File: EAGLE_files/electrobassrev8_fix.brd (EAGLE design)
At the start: 301.8 x 129.5 mm, 234 parts, among them IC1 CY8C58LPXXX, IC18 CY8C4124, IC2 4052D, IC3 LMV321M5, IC5 LMV321M5, IC6 LM324D, J1 105162-0001, J28 PJ-066A, Q1 DMP3099L, U1 ES_DAISY_SEED_DOUBLE, U2 LP2985, U7 ES_DAISY_SEED_DOUBLE, X1 3P-2MM-TH-MALE, X10 3P-2MM-TH-MALE, X11 3P-2MM-TH-MALE, X12 3P-2MM-TH-MALE, X13 3P-2MM-TH-MALE, X14 3P-2MM-TH-MALE, X15 3P-2MM-TH-MALE, X16 332-02, X17 332-02, X18 332-02, X19 332-02, X2 NRJ6HF2, X3 NRJ6HF2, X4 USB+SHIELD, X5 332-02, X6 332-02, X7 332-02, X8 332-02, X9 3P-2MM-TH-MALE

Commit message: changes to how presets are loaded
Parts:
- removed 0_6: (no value), adafruit:1X01
- removed IC1: CY8C58LPXXX, cypress:TQFP100-14X14
- removed JP17, JP18, JP19: PINHD-2X5, Connector:2X05
- removed JP20, JP21: 20021121, custom:20021121
- removed R47, R51, R52, R53, R54: 0R_DNP, adafruit:R0603
- removed U$7: CY8CKIT-059_TARGET_3, CY8KIT-059:CY8CKIT-059_TARGET_3
- added 12VD1: (no value), adafruit:1X01
- added C15, C19, C22, C23, C24, C25: 10uf, rcl:C1206K
- added C16, C31, C32, C33, C36, C45, C46: 1uf, rcl:C0603
- added C17: .001uf, rcl:C0603
- added C18: .01uf, adafruit:C0603K
- added C20, C21: 22uf, rcl:C1206K
- added C26, C28, C30, C40, C41, C42, C43, C44: .1uf, rcl:C0603K
- added C29: 2200pf, adafruit:C0603K
- added J2, J3, J5, J6, J7, J8: SM06B-SRSS-TB(LF)(SN), sm06b:CONN_SM06B-SRSS-TB_JST
- added JP5: 20021121, custom:20021121
- added L1: 2.2uH, Electrosmith-Passives:BOURNS_SRP2010
- added R27, R36: 20k, Resistor:R0603
- added R34, R35: 10k, Resistor:R0603
- added R37: 22R, rcl:R0603
- added R56, R57, R88, R89, R90: 2M, Electrosmith-Passives:R0603
- added R91, R92: 100R, Electrosmith-Passives:R0603
- added R93, R94, R95, R96, R97: 47k, rcl:R0603
- added U$9: POWER_ISOLATE, Electrosmith-IC:XP_POWER_ISEXXXXA
- added U10: OPA1654, Electrosmith-IC:TSSOP-14
- added U3: MCP1755T-5002E/DCSOT-223_5_MCH-M, MCP1755T:SOT-223_5_MCH-M
- added U4: CY8C5888LTI-LP097QFN-68-M, cy8c:QFN-68-M
- added U5: ADUM3160BRWZRW_16_ADI-M, MCP1755T:RW_16_ADI-M
- R23: value 0R -> 2M; device adafruit:R0603 -> Electrosmith-Passives:R0603
- R32: value 1.6k -> 5R_DNP
- R41: value 1.6k -> 22R; device adafruit:R0603 -> rcl:R0603
- R45, R46: value 0R_DNP -> 22R; device adafruit:R0603 -> rcl:R0603
- R50: value 0R -> 5R
- moved R41 113.5 mm to (240.0, 30.0), turned to 0 degrees
- moved R32 99.7 mm to (233.4, 76.2), turned to 90 degrees
- moved C11 59.1 mm to (175.3, 66.5), turned to 270 degrees
- moved R25 56.3 mm to (170.7, 65.5), turned to 180 degrees
- moved C34 55.1 mm to (46.2, 59.9)
- moved R26 52.5 mm to (170.2, 74.7), turned to 180 degrees
- moved C4 52.2 mm to (186.2, 66.5), turned to 270 degrees
- moved C10 50.8 mm to (175.3, 73.7)
- moved R1 47.6 mm to (191.0, 65.8)
- moved C9 45.5 mm to (185.9, 73.9)
- moved J1 45.2 mm to (241.0, 93.5), turned to 180 degrees
- moved R23 41.1 mm to (198.4, 54.6), turned to 270 degrees
- moved R24 37.4 mm to (190.8, 75.2)
- moved AGND5 32.7 mm to (147.1, 59.4)
- moved JP23 32.5 mm to (75.4, 64.0), turned to 270 degrees
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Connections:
- net N$66 renamed ADC4OPAMPOUT
- removed net ADC1_2: R53.1, U7.22, U7.B22
- removed net ADC2_2: R51.1, U7.23, U7.B23
- removed net ADC3_2: R54.1, U7.24, U7.B24
- removed net ADC4_2: R52.1, U7.25, U7.B25
- removed net ADC5_1: U1.26, U1.B26
- removed net ADC5_2: U7.26, U7.B26
- removed net ADC6_1: U1.27, U1.B27
- removed net ADC6_2: U7.27, U7.B27
- removed net ADC7_1: U1.28, U1.B28
- removed net ADC7_2: U7.28, U7.B28
- removed net ADC8_1: U1.29, U1.B29
- removed net ADC8_2: U7.29, U7.B29
- removed net DAISY_D+: R45.1, U7.37, U7.B37
- removed net DAISY_D-: R47.1, U7.36, U7.B36
- removed net EXTRA_GPIO: 0_6.1, U$7.31
- removed net PA0_VBUS: R23.1, U7.32, U7.B32
- removed net PICKUP2_OUT: JP19.2, JP21.10, JP21.9
- removed net PICKUP3_OUT: JP19.3, JP21.7, JP21.8
- removed net SCL_GN: R41.2, U1.12, U1.B12, U7.12, U7.B12
- removed net SDA_GN: R32.2, U1.13, U1.B13, U7.13, U7.B13
- removed net VCCA: IC1.63
- removed net VCCD: IC1.39, IC1.86
- removed net VDDA: IC1.65
- removed net VDDD: IC1.37, IC1.88
- removed net VSSA: IC1.64
- removed net VSSB: IC1.10
- removed net VSSD: IC1.14, IC1.38, IC1.66, IC1.87
- new net +5V_ISOL: C20.1, C28.1, R23.2, R88.2, U$9.P$5, U10.4
- new net 5V0: C15.1, C16.1, C17.1, C18.1, C21.1, L1.P$1, U3.4
- new net ADC1OPAMPOUT: C4.2, IC6.1, R1.1, R81.2
- new net ADC2OPAMPOUT: C9.2, IC6.7, R24.1, R80.2
- new net ADC3OPAMPOUT: C10.2, IC6.8, R26.1, R83.2
- new net ADCBYPASS: C31.1, U4.51
- new net AGND4: G1.1, JP15.4, JP15.6, X2.S
- new net CMOD_CH0: C29.1, U4.60
- new net GNDINT: C20.2, C28.2, JP1.4, JP4.10, R32.1, R34.2, R35.2, R56.1, R57.1, R89.1, R90.1, U$9.P$4, U10.11
- new net GNDINT_KNOBS: JP3.10, U$2.P$3, U$2.P$6
- new net GNDIO: C30.2, JP1.8, JP22.4, U5.2, U5.8
- new net LOUT_2_INTOCN: C24.2, JP4.4, R57.2
- new net N$20: R35.1, R36.2, U10.6
- new net N$21: S1.1, S1.4
- new net N$23: R37.1, U5.6
- new net N$24: R41.1, U5.7
- new net N$63: R45.2, U5.11
- new net N$64: R46.2, U5.10
- new net N$76: R27.1, R91.2, U10.1
- new net N$77: C23.2, R88.1, R89.2, U10.5
- new net N$78: R36.1, R92.2, U10.7
- new net N$79: C24.1, R91.1
- new net N$80: C25.1, R92.1
- new net N$81: C19.1, L1.P$2, U$9.P$2
- new net PROG_RESET: JP5.10, U4.10
- new net PROG_SWDCLK: JP5.4, U4.12
- new net PROG_SWDIO: JP5.2, U4.11
- new net PROG_SWO: JP5.6, U4.14
- new net ROUT_2_INTOCN: C25.2, JP4.2, R90.2
- new net SPI_READY: U1.7, U1.B7, U4.55, U7.1, U7.B1
- new net USBDM: R45.1, U4.23
- new net USBDP: R46.1, U4.22
- new net VCCA_1: C32.1, C42.1, U4.42
- new net VCCD_1: C36.1, C40.1, U4.26, U4.57
- net +10V: now also J2.3, J2.4, J3.3, J3.4; no longer JP18.7, JP18.9
- net +3V3: now also C26.1, C43.1, C44.1, C45.1, C46.1, R93.2, R94.2, R95.2, R96.2, R97.2, U4.17, U4.24, U4.35, U4.52, U4.59, U4.67, U5.12, U5.13, U5.14, U5.16; no longer R32.1, R41.1, U$7.26, U$7.27
- net 12VD1: now also 12VD1.1, U3.1, U3.2
- net 3V3A1: now also C33.1, C41.1, U4.44; no longer R46.1
- net 3V3FORPEDAL: now also JP1.9; no longer JP1.7
- net ADC1_1: no longer C4.2, IC6.1, R1.1, R53.2, R81.2
- net ADC2_1: no longer C9.2, IC6.7, R24.1, R51.2, R80.2
- net ADC3_1: no longer C10.2, IC6.8, R26.1, R54.2, R83.2
- net ADC4_1: no longer R52.2
- net AGND: now also C15.2, C16.2, C17.2, C18.2, C19.2, C21.2, C31.2, C32.2, C33.2, C41.2, C42.2, J2.2, J2.5, J3.2, J3.5, JP1.7, R32.2, U$9.P$1, U3.3, U4.43; no longer JP1.4, JP1.8, JP18.10, JP18.8, JP4.10, S1.1, S1.4
- net AGND3: now also JP15.7; no longer G1.1, JP15.4, JP15.6, X2.S
- net BLUE_LED: now also U4.63; no longer U$7.2
- net CAP_0_0: now also U4.62; no longer U$7.1
- net CAP_0_1: now also U4.64; no longer U$7.3
- net CAP_0_2: now also U4.66; no longer U$7.5
- net CAP_0_3: now also U4.1; no longer U$7.7
- net CAP_1_0: now also U4.29; no longer U$7.51
- net CAP_1_1: now also U4.32; no longer U$7.48
- net CAP_1_2: now also U4.34; no longer U$7.46
- net CAP_1_3: now also U4.37; no longer U$7.44
- net CMOD_CH1: now also U4.15; no longer U$7.21
- net CV_PEDAL: now also U4.33; no longer U$7.47
- net CV_PEDAL_SENSE: now also U4.31; no longer U$7.49
- net DGND: now also C26.2, C29.2, C36.2, C40.2, C43.2, C44.2, C45.2, C46.2, JP5.3, JP5.5, JP5.7, JP5.9, U4.25, U4.45, U4.5, U4.58, U4.69, U4.7, U4.8, U4.9, U5.15, U5.9; no longer JP1.9, JP22.4, U$7.25, U$7.28, U$7.52
- net DGND3: no longer JP15.9
- net DM: now also R37.2; no longer R47.2
- net DOWN: now also U4.41; no longer U$7.40
- net DP: now also R41.2; no longer R45.2
- net EDIT: now also U4.40; no longer U$7.41
- net EXT_MUX_EN: now also U4.61; no longer U$7.38
- net EXT_MUX_S0: now also U4.27; no longer U$7.43
- net EXT_MUX_S1: now also U4.28; no longer U$7.42
- net FRETTED_LATCHING: now also U4.47; no longer U$7.13
- net FRETTED_MOMENTARY: now also U4.46; no longer U$7.14
- net IDAC_OUT: now also U4.56; no longer U$7.30
- net JOY_X: now also U4.68; no longer U$7.6
- net JOY_Y: now also U4.65; no longer U$7.4
- net KNOB_1: now also U4.49; no longer U$7.36
- net KNOB_2: now also U4.36; no longer U$7.45
- net LED_1: now also U4.50; no longer U$7.35
- net LOUT_2: now also C22.1; no longer JP4.4
- net MISO_1: now also U4.19; no longer U$7.24
- net MISO_2: now also U4.2; no longer U$7.8
- net MOSI_1_P: now also U4.20; no longer U$7.10
- net MOSI_2_P: now also U4.3; no longer U$7.12
- net N$45: no longer R46.2
- net N$56: now also JP15.9; no longer JP15.7
- net N$7: now also C22.2, R23.1, R56.2, U10.3; no longer U1.33, U1.B33, U7.33, U7.B33
- net N$8: now also R27.2, R34.1, U10.2; no longer U1.34, U1.B34, U7.34, U7.B34
- net OUTGND: no longer JP3.10, U$2.P$3, U$2.P$6
- net PICKUP1: now also J3.6; no longer JP18.1
- net PICKUP1_OUT: now also J6.6; no longer JP19.1
- net PICKUP1_OUT2: now also J7.6; no longer JP17.1
- net PICKUP2: now also J2.6; no longer JP18.2
- net PICKUP2_OUT2: now also J8.6; no longer JP17.2
- net PICKUP2_OUT_HIGH: now also J5.6; no longer JP20.10, JP20.9
- net PICKUP3: now also J2.1; no longer JP18.3
- net PICKUP3_OUT2: now also J8.1; no longer JP17.3
- net PICKUP3_OUT_HIGH: now also J5.1; no longer JP20.7, JP20.8
- net PICKUP4: now also J3.1; no longer JP18.4
- net PICKUP4_OUT: now also J6.1; no longer JP19.4
- net PICKUP4_OUT2: now also J7.1; no longer JP17.4
- net PICKUP_GND1: now also J6.2, J6.5; no longer JP19.10, JP19.8, JP21.1, JP21.2, JP21.3, JP21.4
- net PICKUP_GND1_HIGH: now also J5.2, J5.5; no longer JP20.1, JP20.2, JP20.3, JP20.4
- net PICKUP_GND2: now also J7.2, J7.5, J8.2, J8.5; no longer JP17.10, JP17.8
- net PICKUP_PWR1: now also J6.3, J6.4; no longer JP19.7, JP19.9, JP21.5, JP21.6
- net PICKUP_PWR1_HIGH: now also J5.3, J5.4; no longer JP20.5, JP20.6
- net PICKUP_PWR2: now also J7.3, J7.4, J8.3, J8.4; no longer JP17.7, JP17.9
- net ROUT_2: now also C23.1; no longer JP4.2
- net SCL: now also U4.38; no longer U$7.16
- net SCLK_1_P: now also U4.18; no longer U$7.23
- net SCLK_2_P: now also U4.4; no longer U$7.11
- net SDA: now also U4.39; no longer U$7.15
- net SD_CMD: now also R95.1
- net SD_DAT0: now also R94.1
- net SD_DAT1: now also R93.1
- net SD_DAT2: now also R97.1
- net SD_DAT3: now also R96.1
- net SS_1_P: now also U4.16; no longer U$7.22
- net SS_2_P: now also U4.13; no longer U$7.19
- net UP: now also U4.30; no longer U$7.50
- net VBUS: now also C30.1, U5.1, U5.3, U5.4, U5.5
- net VBUS_DIVIDED: now also U4.21; no longer R23.2, U$7.9
- net V_H: now also U4.53; no longer U$7.33
- net V_T: now also U4.48, U4.54; no longer U$7.32, U$7.37
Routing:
- net USBDM: track 0.00 -> 273.3 mm, vias 0 -> 1
- net USBDP: track 0.00 -> 272.6 mm, vias 0 -> 1
- net SDA_GN: track 145.0 -> 0.00 mm, vias 2 -> 0
- net SCL_GN: track 138.2 -> 0.00 mm, vias 2 -> 0
- net VBUS_DIVIDED: track 268.2 -> 133.7 mm, vias 3 -> 1
- net N$8: track 115.5 -> 4.79 mm, vias 2 -> 0
- net ADC4_2: track 105.8 -> 0.00 mm
- net MISO_1: track 148.9 -> 50.2 mm, vias 1 -> 2
- net DAISY_D+: track 94.3 -> 0.00 mm, vias 1 -> 0
- net DAISY_D-: track 92.8 -> 0.00 mm, vias 1 -> 0
- net ADC3_2: track 85.6 -> 0.00 mm, vias 2 -> 0
- net +3V3: track 27.6 -> 111.8 mm, vias 7 -> 6
- net SS_2: track 177.0 -> 99.5 mm, vias 3 -> 0
- net N$7: track 114.8 -> 37.4 mm
- net SDA: track 76.1 -> 2.16 mm, vias 2 -> 0
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- added copper zone on layer 15, net +5V_ISOL
- added copper zone on layer 2, net AGND3
- added copper zone on layer 15, net AGND4
- added copper zone on layer 2, net AGND4
- added copper zone on layer 2, net GNDINT
- added copper zone on layer 15, net GNDINT_KNOBS
- added copper zone on layer 2, net GNDINT_KNOBS
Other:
- board size 301.8 x 129.5 mm -> 314.7 x 129.5 mm
- board text added: "rev6"
- board text removed: "rev5"

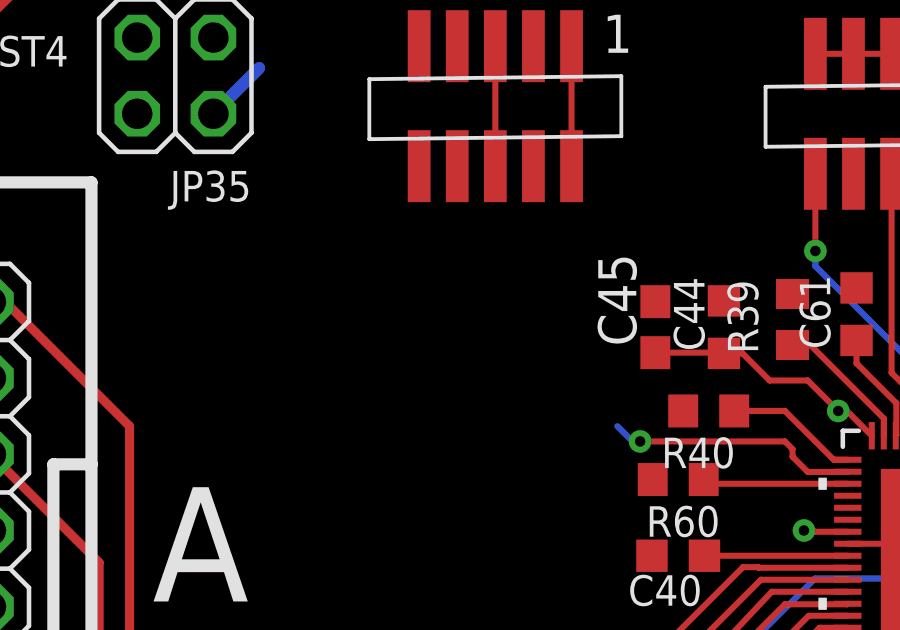
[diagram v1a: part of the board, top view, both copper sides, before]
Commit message: writing multiple presets to an sd card and loading them based on commands from psoc
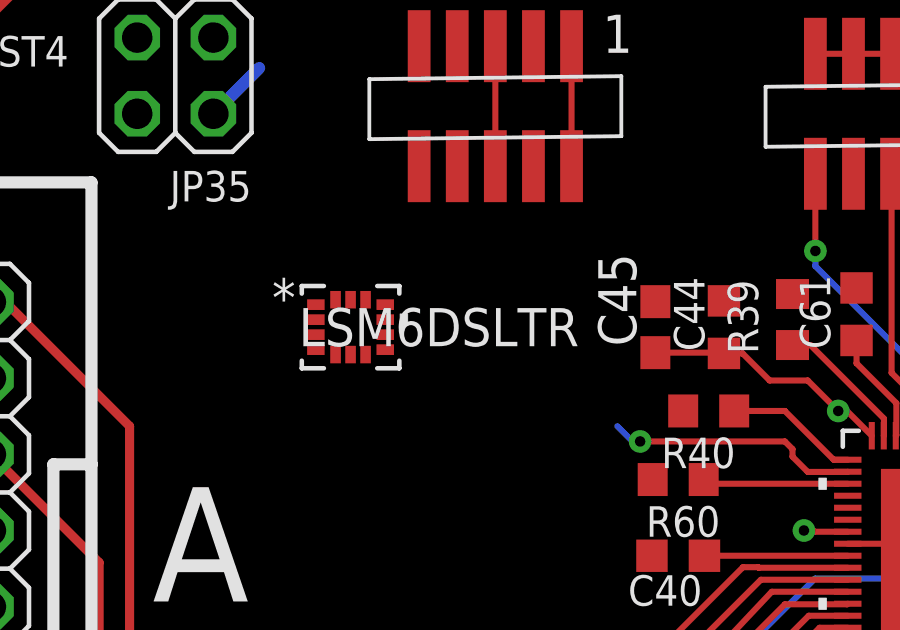
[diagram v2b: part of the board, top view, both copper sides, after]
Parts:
- added U6: LSM6DSLTR, 6dsl:QFN_6DSLTR_STM
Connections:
- new net GND: U6.7
- new net GND_2: U6.6
- new net VDD: U6.8
- new net VDDIO: U6.5
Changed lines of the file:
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@@
 <attribute name="VALUE" x="56.769" y="60.579" size="1.27" layer="27" rot="R270"/>
 </element>
+<element name="U6" library="6dsl" package="QFN_6DSLTR_STM" value="LSM6DSLTR" x="31.242" y="76.2" smashed="yes">
+<attribute name="COPYRIGHT" value="Copyright (C) 2022 Ultra Librarian. All rights reserved." x="31.242" y="76.2" size="1.778" layer="27" display="off"/>
+<attribute name="DIGI-KEY_PART_NUMBER_1" value="497-16705-2-ND" x="31.242" y="76.2" size="1.778" layer="27" display="off"/>
+<attribute name="DIGI-KEY_PART_NUMBER_2" value="497-16705-1-ND" x="31.242" y="76.2" size="1.778" layer="27" display="off"/>
+<attribute name="DIGI-KEY_PART_NUMBER_3" value="497-16705-6-ND" x="31.242" y="76.2" size="1.778" layer="27" display="off"/>
+<attribute name="MANUFACTURER_PART_NUMBER" value="LSM6DSLTR" x="31.242" y="76.2" size="1.778" layer="27" display="off"/>
+<attribute name="MFR_NAME" value="STMicroelectronics" x="31.242" y="76.2" size="1.778" layer="27" display="off"/>
+<attribute name="NAME" x="27.9654" y="75.565" size="1.27" layer="27" ratio="6" rot="SR0"/>
+<attribute name="VALUE" x="29.5148" y="75.565" size="1.27" layer="21" ratio="6" rot="SR0"/>
+</element>
 </elements>
 <signals>
@@
 <vertex x="29.89033125" y="59.671296875"/>
 <vertex x="91.186" y="60.96"/>
-<vertex x="91.186" y="60.96"/>
 <vertex x="102.86698125" y="60.706"/>
 <vertex x="109.976709375" y="65.30963125"/>
@@
 <wire x1="47.8155" y1="68.58" x2="55.8165" y2="67.38" width="0" layer="19" extent="1-1"/>
 </signal>
+<signal name="VDDIO">
+<contactref element="U6" pad="5"/>
+</signal>
+<signal name="GND_2">
+<contactref element="U6" pad="6"/>
+</signal>
+<signal name="GND">
+<contactref element="U6" pad="7"/>
+</signal>
+<signal name="VDD">
+<contactref element="U6" pad="8"/>
+</signal>
 </signals>
